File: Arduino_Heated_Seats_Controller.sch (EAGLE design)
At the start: 26 parts, among them U1 MEGA8-AI, U3 ULN2003AN, U4 M54564FP

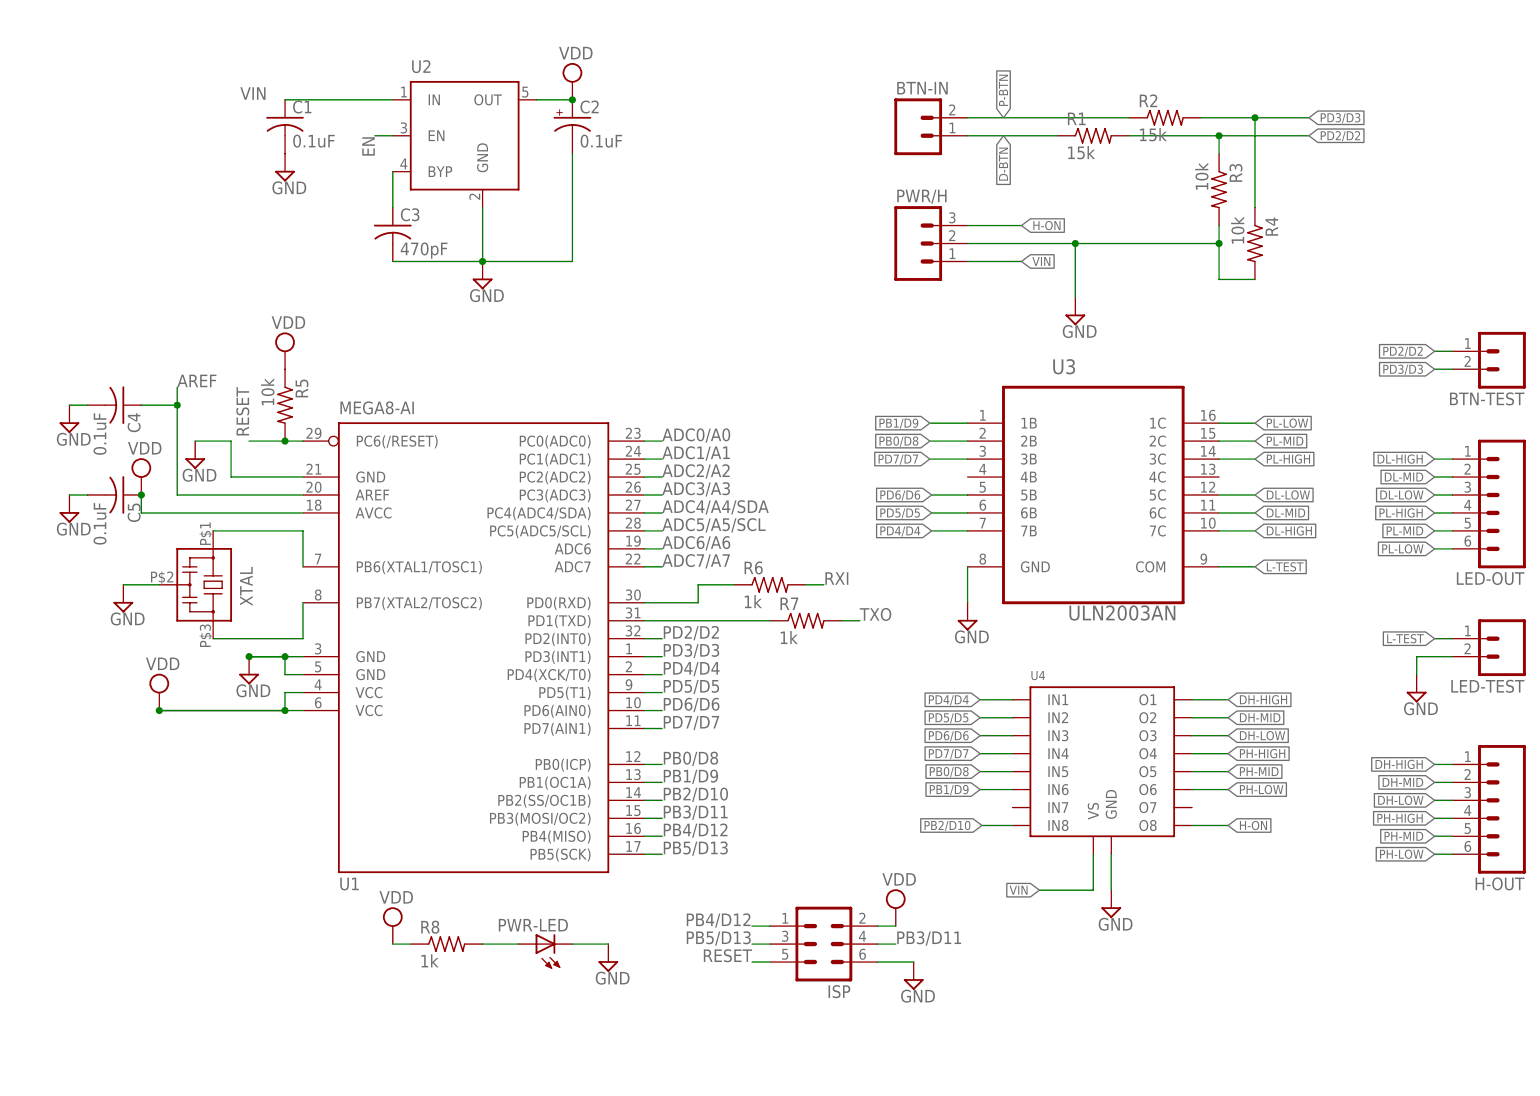
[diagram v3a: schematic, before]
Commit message: Settled for an ULN2003A (compatible with Toshiba variant) and the TD62783AFG (from Toshiba as well).
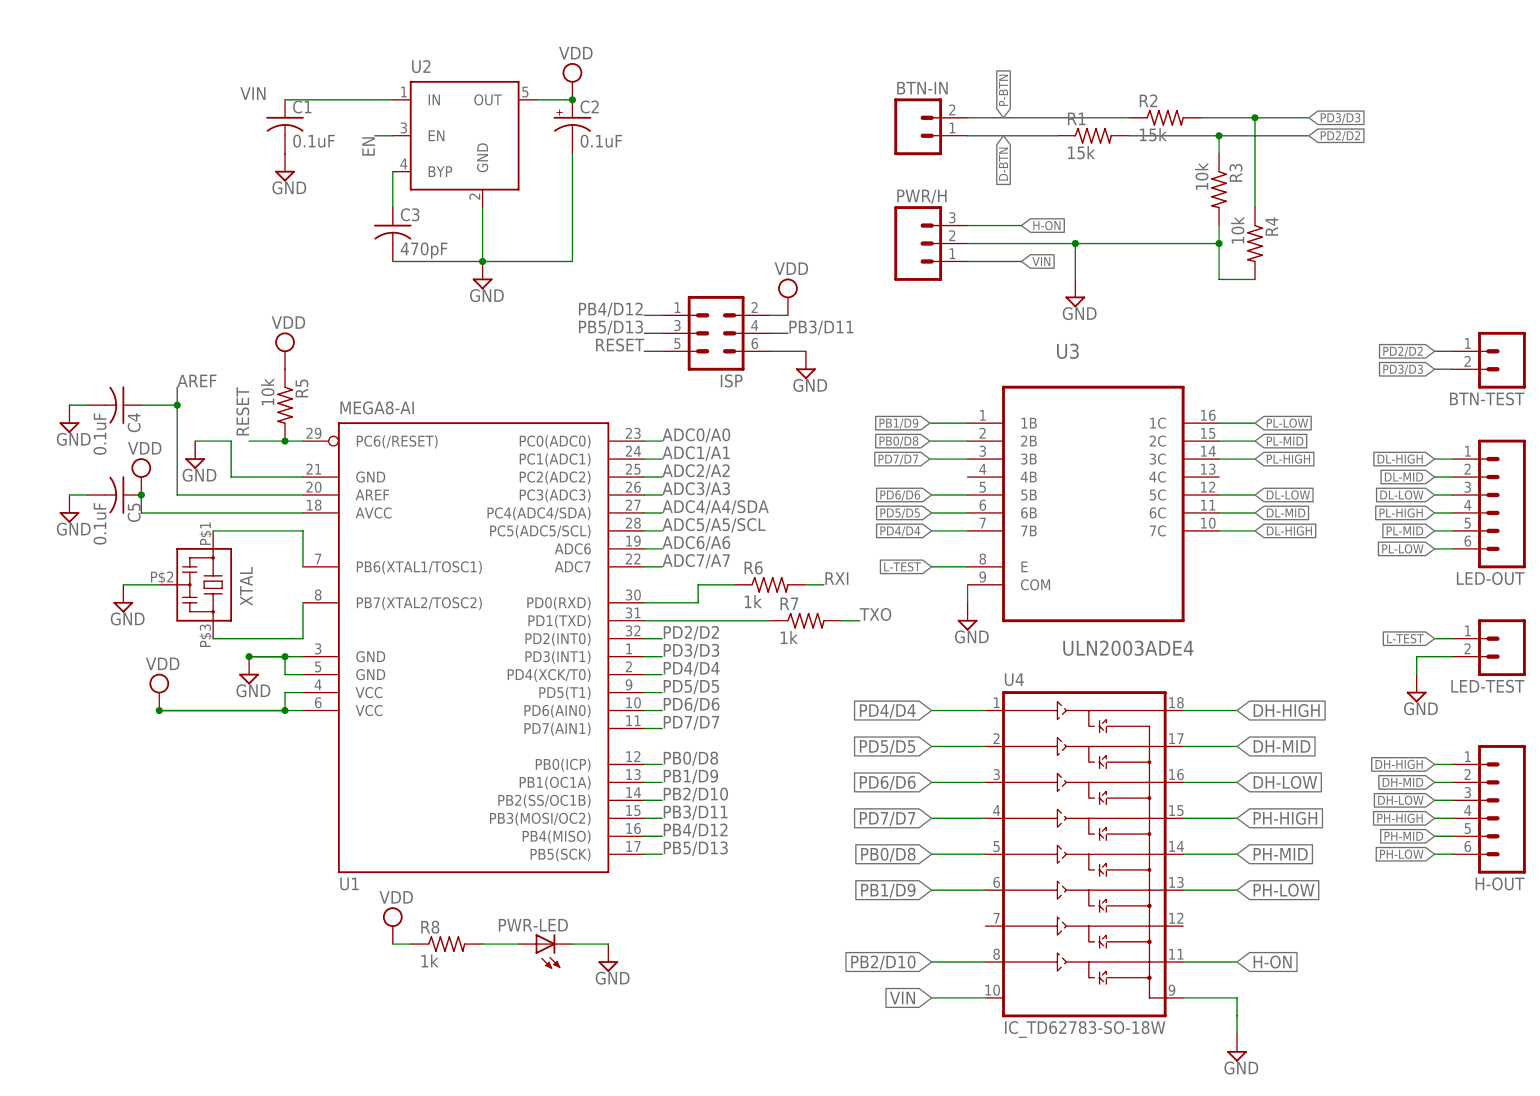
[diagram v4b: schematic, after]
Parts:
- U3: value ULN2003AN -> ULN2003ADE4; device Texas Instruments_By_element14_Batch_1:ULN2003ANE4 -> Texas Instruments_By_element14_Batch_1:ULN2003ADE4
- U4: value M54564FP -> IC_TD62783-SO-18W; device M54564P-FP:M54564FP -> dp_devices:IC_TD62783-SO-18W
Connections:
- net DH-HIGH: now also U4.OUT1; no longer U4.O1
- net DH-LOW: now also U4.OUT3; no longer U4.O3
- net DH-MID: now also U4.OUT2; no longer U4.O2
- net GND: now also U3.COM; no longer U3.GND
- net H-ON: now also U4.OUT8; no longer U4.O8
- net L-TEST: now also U3.E; no longer U3.COM
- net PH-HIGH: now also U4.OUT4; no longer U4.O4
- net PH-LOW: now also U4.OUT6; no longer U4.O6
- net PH-MID: now also U4.OUT5; no longer U4.O5
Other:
- moved on the sheet: ISP, U3

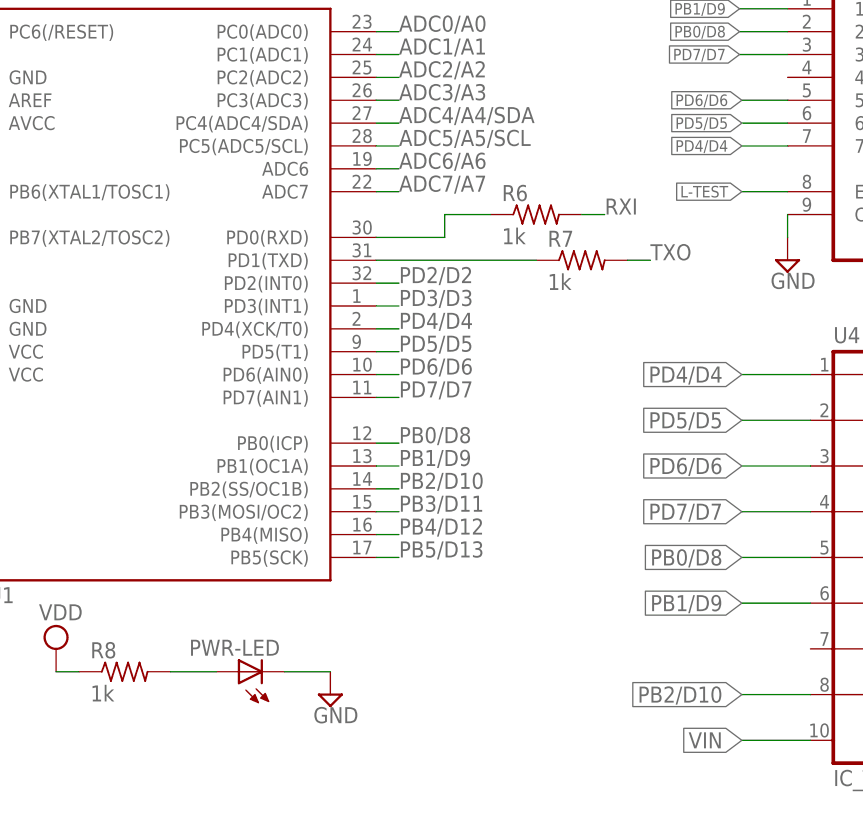
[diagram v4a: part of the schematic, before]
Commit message: Additional pads for TX and RX (if needed).
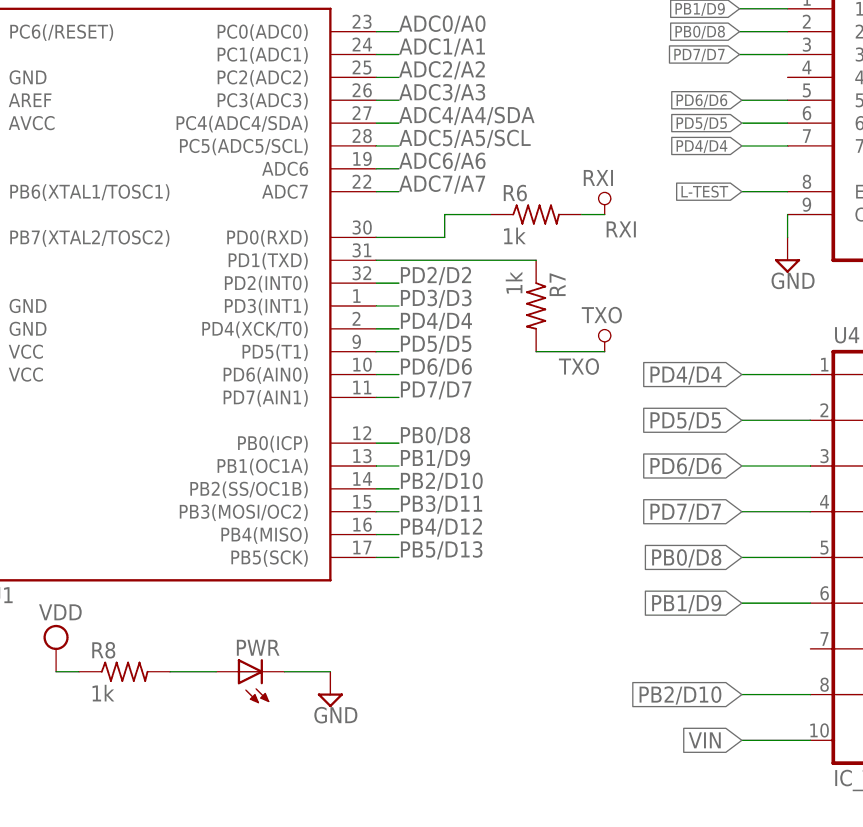
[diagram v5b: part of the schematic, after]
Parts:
- added RXI, TXO: PAD_TERMINAL-1.02MM_SQUARE, dp_devices:PAD_TERMINAL-1.02MM_SQUARE
- renumbered PWR-LED to PWR
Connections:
- net RXI: now also RXI.P
- net TXO: now also TXO.P
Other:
- moved on the sheet: R7
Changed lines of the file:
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@@
 <part name="C1" library="rcl" deviceset="C-US" device="C0603" value="0.1uF"/>
 <part name="SUPPLY13" library="supply2" deviceset="GND" device=""/>
-<part name="PWR-LED" library="led" deviceset="LED" device="CHIP-LED0603"/>
+<part name="PWR" library="led" deviceset="LED" device="CHIP-LED0603"/>
 <part name="R8" library="resistor" deviceset="R-US_" device="R0603" value="1k"/>
 <part name="SUPPLY14" library="supply2" deviceset="GND" device=""/>
@@
 <part name="SUPPLY20" library="supply2" deviceset="GND" device=""/>
 <part name="U3" library="Texas Instruments_By_element14_Batch_1" deviceset="ULN2003ADE4" device=""/>
+<part name="RXI" library="dp_devices" deviceset="PAD_TERMINAL" device="-1.02MM_SQUARE"/>
+<part name="TXO" library="dp_devices" deviceset="PAD_TERMINAL" device="-1.02MM_SQUARE"/>
 </parts>
 <sheets>
@@
 <instance part="SUPPLY6" gate="G$1" x="25.4" y="53.34"/>
 <instance part="R6" gate="G$1" x="111.76" y="68.58"/>
-<instance part="R7" gate="G$1" x="116.84" y="63.5"/>
+<instance part="R7" gate="G$1" x="111.76" y="58.42" rot="R270"/>
 <instance part="C4" gate="G$1" x="20.32" y="93.98" rot="R270"/>
 <instance part="SUPPLY7" gate="GND" x="12.7" y="91.44"/>
@@
 <instance part="C1" gate="G$1" x="43.18" y="134.62"/>
 <instance part="SUPPLY13" gate="GND" x="43.18" y="127"/>
-<instance part="PWR-LED" gate="G$1" x="78.74" y="17.78" rot="R90"/>
+<instance part="PWR" gate="G$1" x="78.74" y="17.78" rot="R90"/>
 <instance part="R8" gate="G$1" x="66.04" y="17.78"/>
 <instance part="SUPPLY14" gate="GND" x="88.9" y="15.24"/>
@@
 <instance part="SUPPLY20" gate="GND" x="177.8" y="2.54"/>
 <instance part="U3" gate="A" x="157.48" y="83.82"/>
+<instance part="RXI" gate="T" x="119.38" y="71.12"/>
+<instance part="TXO" gate="T" x="119.38" y="55.88"/>
 </instances>
 <busses>
@@
 </segment>
 <segment>
-<pinref part="PWR-LED" gate="G$1" pin="C"/>
+<pinref part="PWR" gate="G$1" pin="C"/>
 <pinref part="SUPPLY14" gate="GND" pin="GND"/>
 <wire x1="83.82" y1="17.78" x2="88.9" y2="17.78" width="0.1524" layer="91"/>
@@
 <segment>
 <wire x1="116.84" y1="68.58" x2="119.38" y2="68.58" width="0.1524" layer="91"/>
-<label x="119.38" y="68.58" size="1.778" layer="95"/>
+<label x="119.38" y="66.04" size="1.778" layer="95"/>
 <pinref part="R6" gate="G$1" pin="2"/>
+<pinref part="RXI" gate="T" pin="P"/>
 </segment>
 </net>
 <net name="TXO" class="0">
 <segment>
-<wire x1="121.92" y1="63.5" x2="124.46" y2="63.5" width="0.1524" layer="91"/>
-<label x="124.46" y="63.5" size="1.778" layer="95"/>
+<wire x1="111.76" y1="53.34" x2="119.38" y2="53.34" width="0.1524" layer="91"/>
+<label x="114.3" y="50.8" size="1.778" layer="95"/>
 <pinref part="R7" gate="G$1" pin="2"/>
+<pinref part="TXO" gate="T" pin="P"/>
 </segment>
 </net>
@@
 <net name="N$3" class="0">
 <segment>
-<pinref part="PWR-LED" gate="G$1" pin="A"/>
+<pinref part="PWR" gate="G$1" pin="A"/>
 <pinref part="R8" gate="G$1" pin="2"/>
 <wire x1="71.12" y1="17.78" x2="76.2" y2="17.78" width="0.1524" layer="91"/>

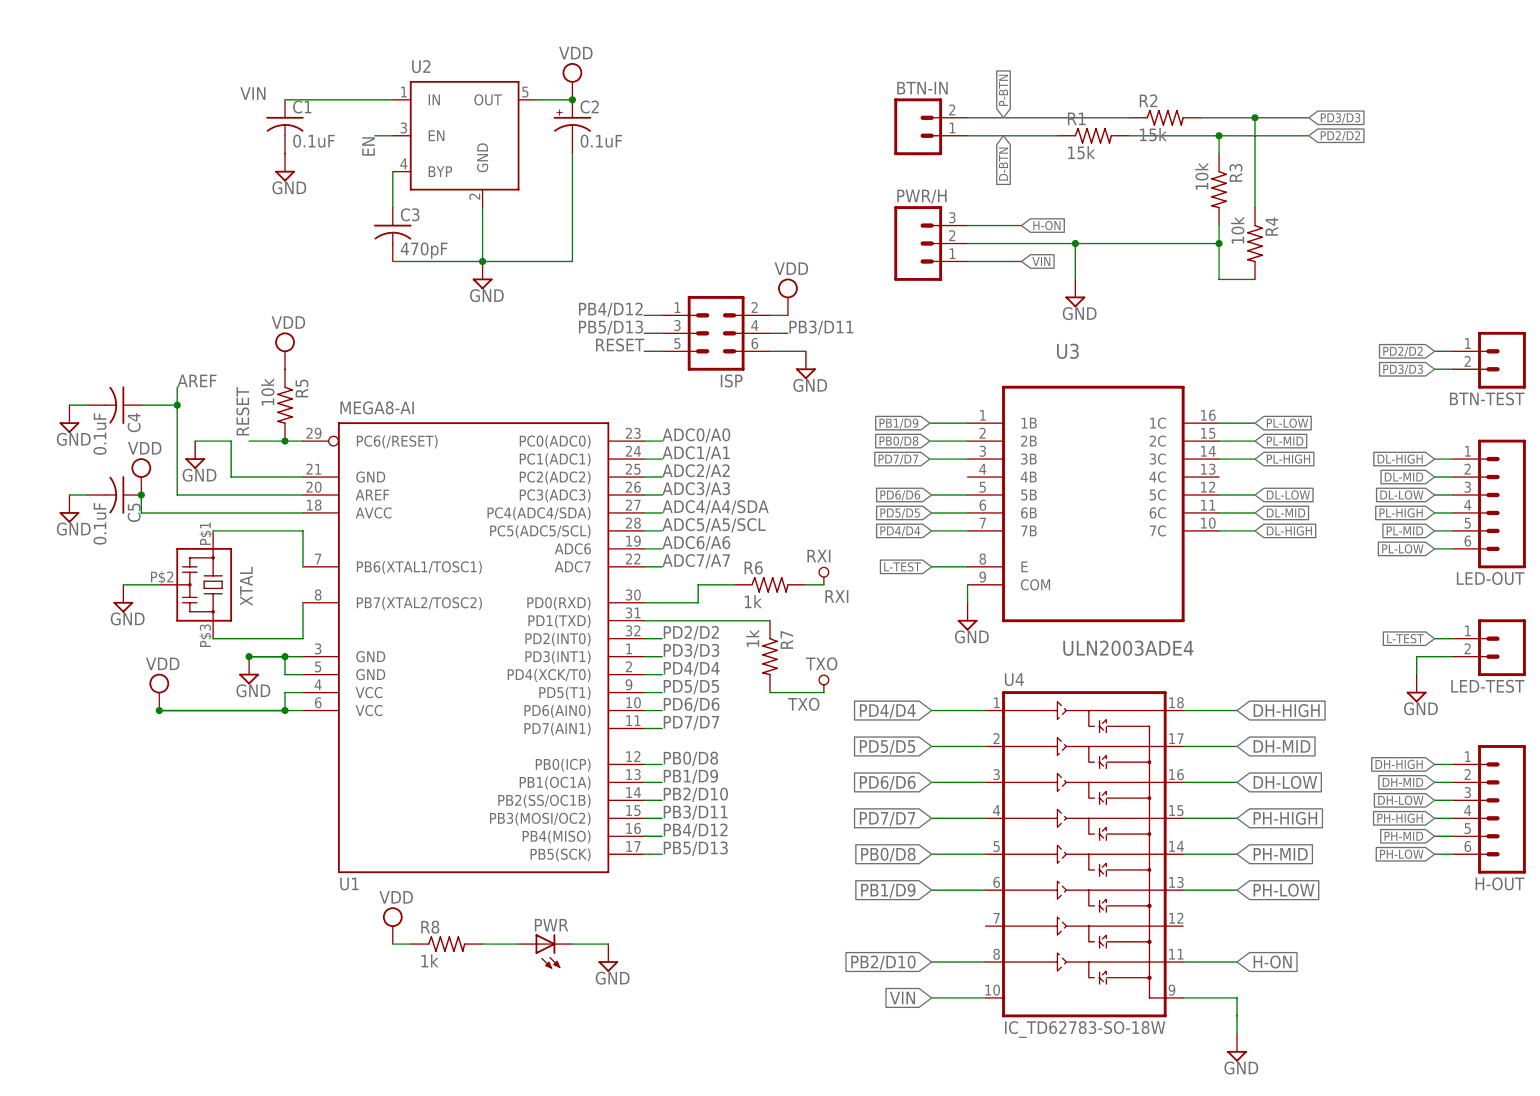
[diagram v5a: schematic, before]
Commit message: Swapped MIC5219B for uA78M05I to handle higher input voltage (and lower operating environment temps). Swapped a few capacitors (removed polarized 0.1uF on regulator output). Removed a few pads not needed for this project.
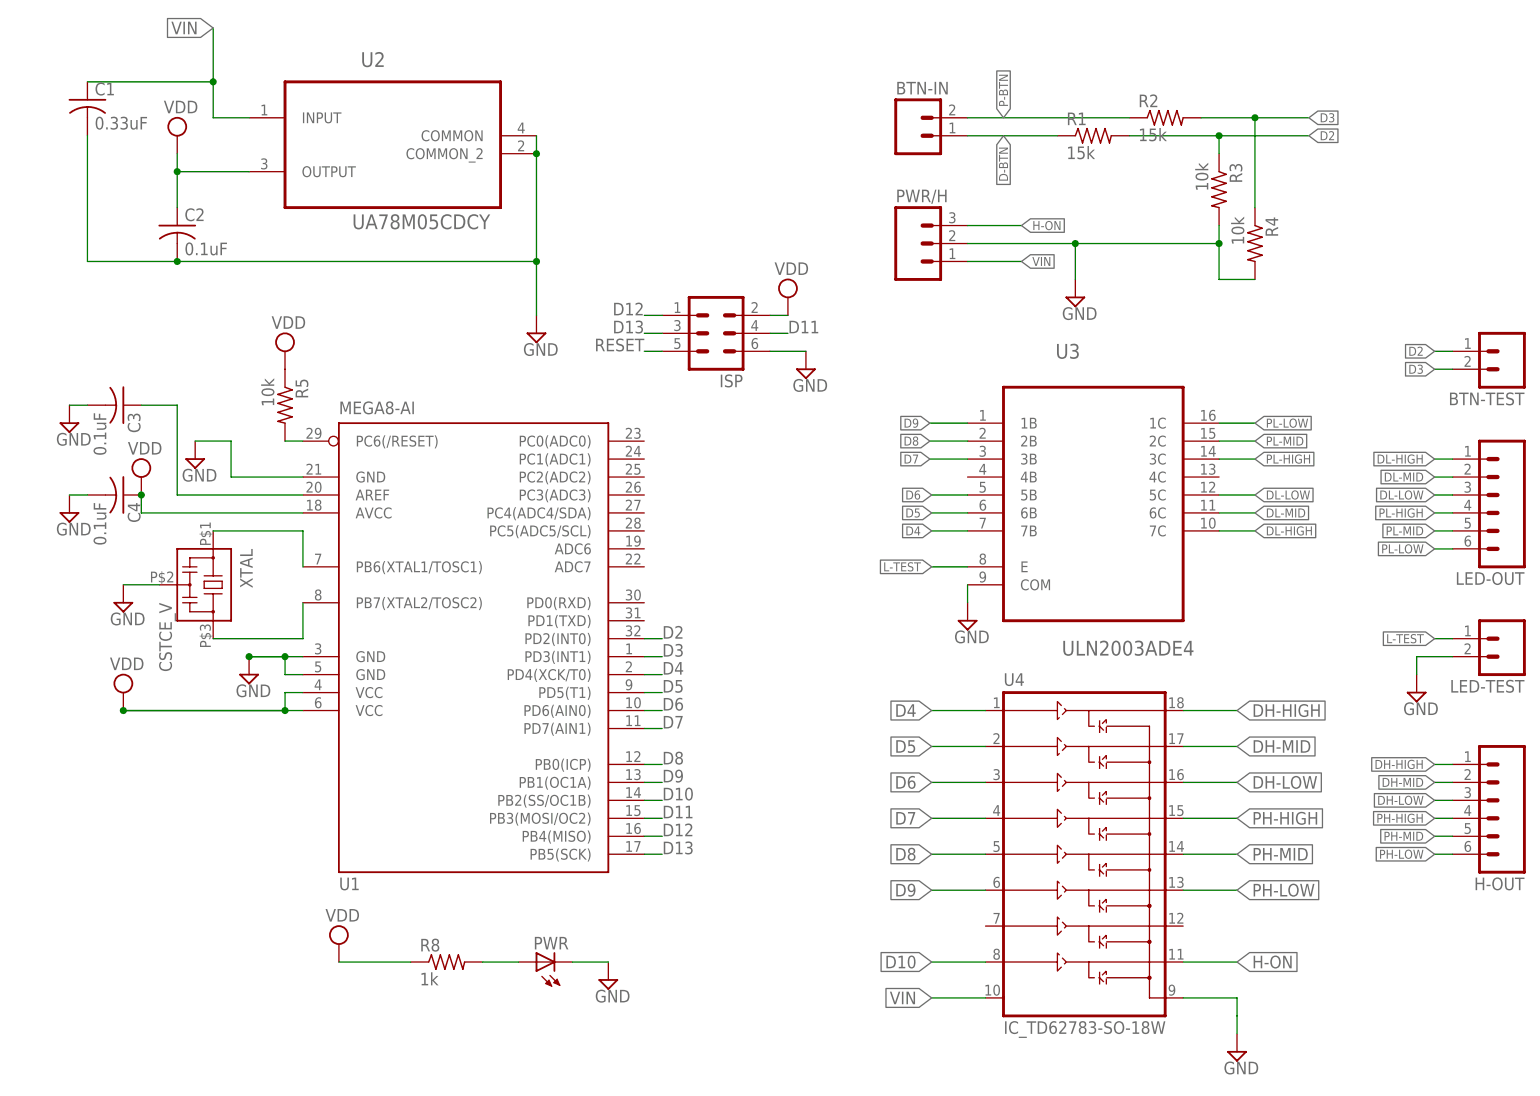
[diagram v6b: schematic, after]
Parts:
- removed C5: 0.1uF, rcl:C-USC0603
- removed R6, R7: 1k, resistor:R-US_R0603
- removed RXI, TXO: PAD_TERMINAL-1.02MM_SQUARE, dp_devices:PAD_TERMINAL-1.02MM_SQUARE
- C1: value 0.1uF -> 0.33uF
- C2: device rcl:CPOL-USCT3216 -> rcl:C-USC0603
- C3: value 470pF -> 0.1uF
- U2: value (none) -> UA78M05CDCY; device v-reg-micrel:MIC5219XX -> Texas Instruments_By_element14_Batch_1:UA78M05CDCY
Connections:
- net PB0/D8 renamed D8
- net PB1/D9 renamed D9
- net PB2/D10 renamed D10
- net PB3/D11 renamed D11
- net PB4/D12 renamed D12
- net PB5/D13 renamed D13
- net PD2/D2 renamed D2
- net PD3/D3 renamed D3
- net PD4/D4 renamed D4
- net PD5/D5 renamed D5
- net PD6/D6 renamed D6
- net PD7/D7 renamed D7
- removed net ADC0/A0: U1.PC0(ADC0)
- removed net ADC1/A1: U1.PC1(ADC1)
- removed net ADC2/A2: U1.PC2(ADC2)
- removed net ADC3/A3: U1.PC3(ADC3)
- removed net ADC4/A4/SDA: U1.PC4(ADC4/SDA)
- removed net ADC5/A5/SCL: U1.PC5(ADC5/SCL)
- removed net ADC6/A6: U1.ADC6
- removed net ADC7/A7: U1.ADC7
- removed net EN: U2.EN
- removed net N$4: C3.1, U2.BYP
- removed net N$8: R6.1, U1.PD0(RXD)
- removed net N$9: R7.1, U1.PD1(TXD)
- removed net RXI: R6.2, RXI.P
- removed net TXO: R7.2, TXO.P
- net AREF: now also C3.1; no longer C4.1
- net GND: now also C2.2, U2.COMMON, U2.COMMON_2; no longer C2.-, C5.2, U2.GND
- net VDD: now also C2.1, C4.1, U2.OUTPUT; no longer C2.+, C5.1, U2.OUT
- net VIN: now also U2.INPUT; no longer U2.IN
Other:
- moved on the sheet: C1, C3, C4, PWR, R8
